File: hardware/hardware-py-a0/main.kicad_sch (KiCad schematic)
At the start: 64 parts, among them J1 Conn_02x08_Odd_Even, J2 USB_C_Receptacle_USB2.0_16P, J3 Conn_02x04_Odd_Even, Q3 AO3401A, Q6 BSS138, Q7 AO3401A, SW1 SW_Push, SW10 SW_Push, SW11 SW_Push, SW12 SW_Push, SW13 SW_Push, SW14 SW_Push, SW15 SW_Push, SW16 SW_Push, SW17 SW_Push, SW18 SW_Push, SW19 SW_Push, SW2 SW_Push, SW20 SW_Push, SW21 Encoder, SW22 RST, SW3 SW_Push, SW4 SW_Push, SW5 SW_Push, SW6 SW_Push, SW7 SW_Push, SW8 SW_Push, SW9 SW_Push, U3 74HC595, U4 ESP32-S3-WROOM-1

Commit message: [dev] py-a0 board files
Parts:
- added C4: 1u, Capacitor_SMD:C_1206_3216Metric, symbol Device:C
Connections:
- net GND: now also C4.2
- net RST: now also C4.1
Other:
- moved on the sheet: SW22
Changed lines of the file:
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@@
 	)
 	(junction
+		(at 147.32 105.41)
+		(diameter 0)
+		(color 0 0 0 0)
+	)
+	(junction
+		(at 139.7 105.41)
+		(diameter 0)
+		(color 0 0 0 0)
+	)
+	(junction
 		(at 190.5 50.8)
 		(diameter 0)
@@
 	)
 	(junction
+		(at 160.02 114.3)
+		(diameter 0)
+		(color 0 0 0 0)
+	)
+	(junction
 		(at 210.82 50.8)
 		(diameter 0)
@@
 	(wire
 		(pts
+			(xy 160.02 114.3) (xy 147.32 114.3)
+		)
+		(stroke
+			(width 0)
+			(type default)
+		)
+	)
+	(wire
+		(pts
 			(xy 71.12 64.77) (xy 71.12 60.96)
 		)
@@
 	(wire
 		(pts
-			(xy 139.7 102.87) (xy 139.7 114.3)
+			(xy 139.7 104.14) (xy 139.7 105.41)
 		)
 		(stroke
@@
 	(wire
 		(pts
+			(xy 139.7 105.41) (xy 139.7 114.3)
+		)
+		(stroke
+			(width 0)
+			(type default)
+		)
+	)
+	(wire
+		(pts
 			(xy 91.44 54.61) (xy 91.44 50.8)
 		)
@@
 	(wire
 		(pts
+			(xy 149.86 105.41) (xy 147.32 105.41)
+		)
+		(stroke
+			(width 0)
+			(type default)
+		)
+	)
+	(wire
+		(pts
 			(xy 124.46 114.3) (xy 127 114.3)
 		)
@@
 	(wire
 		(pts
-			(xy 151.13 114.3) (xy 149.86 114.3)
+			(xy 147.32 105.41) (xy 139.7 105.41)
 		)
 		(stroke
@@
 	(wire
 		(pts
+			(xy 160.02 114.3) (xy 160.02 105.41)
+		)
+		(stroke
+			(width 0)
+			(type default)
+		)
+	)
+	(wire
+		(pts
 			(xy 119.38 102.87) (xy 124.46 102.87)
 		)
@@
 	(wire
 		(pts
+			(xy 147.32 114.3) (xy 147.32 113.03)
+		)
+		(stroke
+			(width 0)
+			(type default)
+		)
+	)
+	(wire
+		(pts
 			(xy 186.69 134.62) (xy 170.18 134.62)
 		)
@@
 	(hierarchical_label "RST"
 		(shape input)
-		(at 139.7 102.87 0)
+		(at 139.7 104.14 90)
 		(fields_autoplaced yes)
 		(effects
@@
 	(symbol
 		(lib_id "Switch:SW_Push")
-		(at 144.78 114.3 0)
+		(at 154.94 105.41 0)
 		(unit 1)
 		(exclude_from_sim no)
@@
 		(fields_autoplaced yes)
 		(property "Reference" "SW22"
-			(at 144.78 106.68 0)
+			(at 154.94 97.79 0)
 			(effects
 				(font
@@
 		)
 		(property "Value" "RST"
-			(at 144.78 109.22 0)
+			(at 154.94 100.33 0)
 			(effects
 				(font
@@
 		)
 		(property "Footprint" "Button_Switch_SMD:SW_SPST_PTS647_Sx38"
-			(at 144.78 109.22 0)
+			(at 154.94 100.33 0)
 			(effects
 				(font
@@
 		)
 		(property "Datasheet" "~"
-			(at 144.78 109.22 0)
+			(at 154.94 100.33 0)
 			(effects
 				(font
@@
 		)
 		(property "Description" "Push button switch, generic, two pins"
-			(at 144.78 114.3 0)
+			(at 154.94 105.41 0)
 			(effects
 				(font
@@
 	(symbol
 		(lib_id "power:GND")
-		(at 151.13 114.3 0)
+		(at 160.02 114.3 0)
 		(mirror y)
 		(unit 1)
@@
 		(dnp no)
 		(property "Reference" "#PWR06"
-			(at 151.13 120.65 0)
+			(at 160.02 120.65 0)
 			(effects
 				(font
@@
 		)
 		(property "Value" "GND"
-			(at 153.67 114.3 0)
+			(at 162.56 114.3 0)
 			(effects
 				(font
@@
 		)
 		(property "Footprint" ""
-			(at 151.13 114.3 0)
+			(at 160.02 114.3 0)
 			(effects
 				(font
@@
 		)
 		(property "Datasheet" ""
-			(at 151.13 114.3 0)
+			(at 160.02 114.3 0)
 			(effects
 				(font
@@
 		)
 		(property "Description" "Power symbol creates a global label with name \"GND\" , ground"
-			(at 151.13 114.3 0)
+			(at 160.02 114.3 0)
 			(effects
 				(font
@@
 					(unit 1)
 				)
+			)
+		)
+	)
+	(symbol
+		(lib_id "Device:C")
+		(at 147.32 109.22 0)
+		(unit 1)
+		(exclude_from_sim no)
+		(in_bom yes)
+		(on_board yes)
+		(dnp no)
+		(property "Reference" "C4"
+			(at 146.558 103.632 0)
+			(effects
+				(font
+					(size 1.27 1.27)
+				)
+				(justify left)
+			)
+		)
+		(property "Value" "1u"
+			(at 148.082 112.268 0)
+			(effects
+				(font
+					(size 1.27 1.27)
+				)
+				(justify left)
+			)
+		)
+		(property "Footprint" "Capacitor_SMD:C_1206_3216Metric"
+			(at 148.2852 113.03 0)
+			(effects
+				(font
+					(size 1.27 1.27)
+				)
+				(hide yes)
+			)
+		)
+		(property "Datasheet" "~"
+			(at 147.32 109.22 0)
+			(effects
+				(font
+					(size 1.27 1.27)
+				)
+				(hide yes)
+			)
+		)
+		(property "Description" "Unpolarized capacitor"
+			(at 147.32 109.22 0)
+			(effects
+				(font
+					(size 1.27 1.27)
+				)
+				(hide yes)
+			)
+		)
+		(pin "2"
+		)
+		(pin "1"
+		)
+		(instances
+			(project "numcalcium"
+				(path "/842c0813-91d3-4f68-bc1f-ac3ce07be478/b6a1d74e-f5bd-4c1c-9567-b593baf30f34"
+					(reference "C4")
+					(unit 1)
+				)

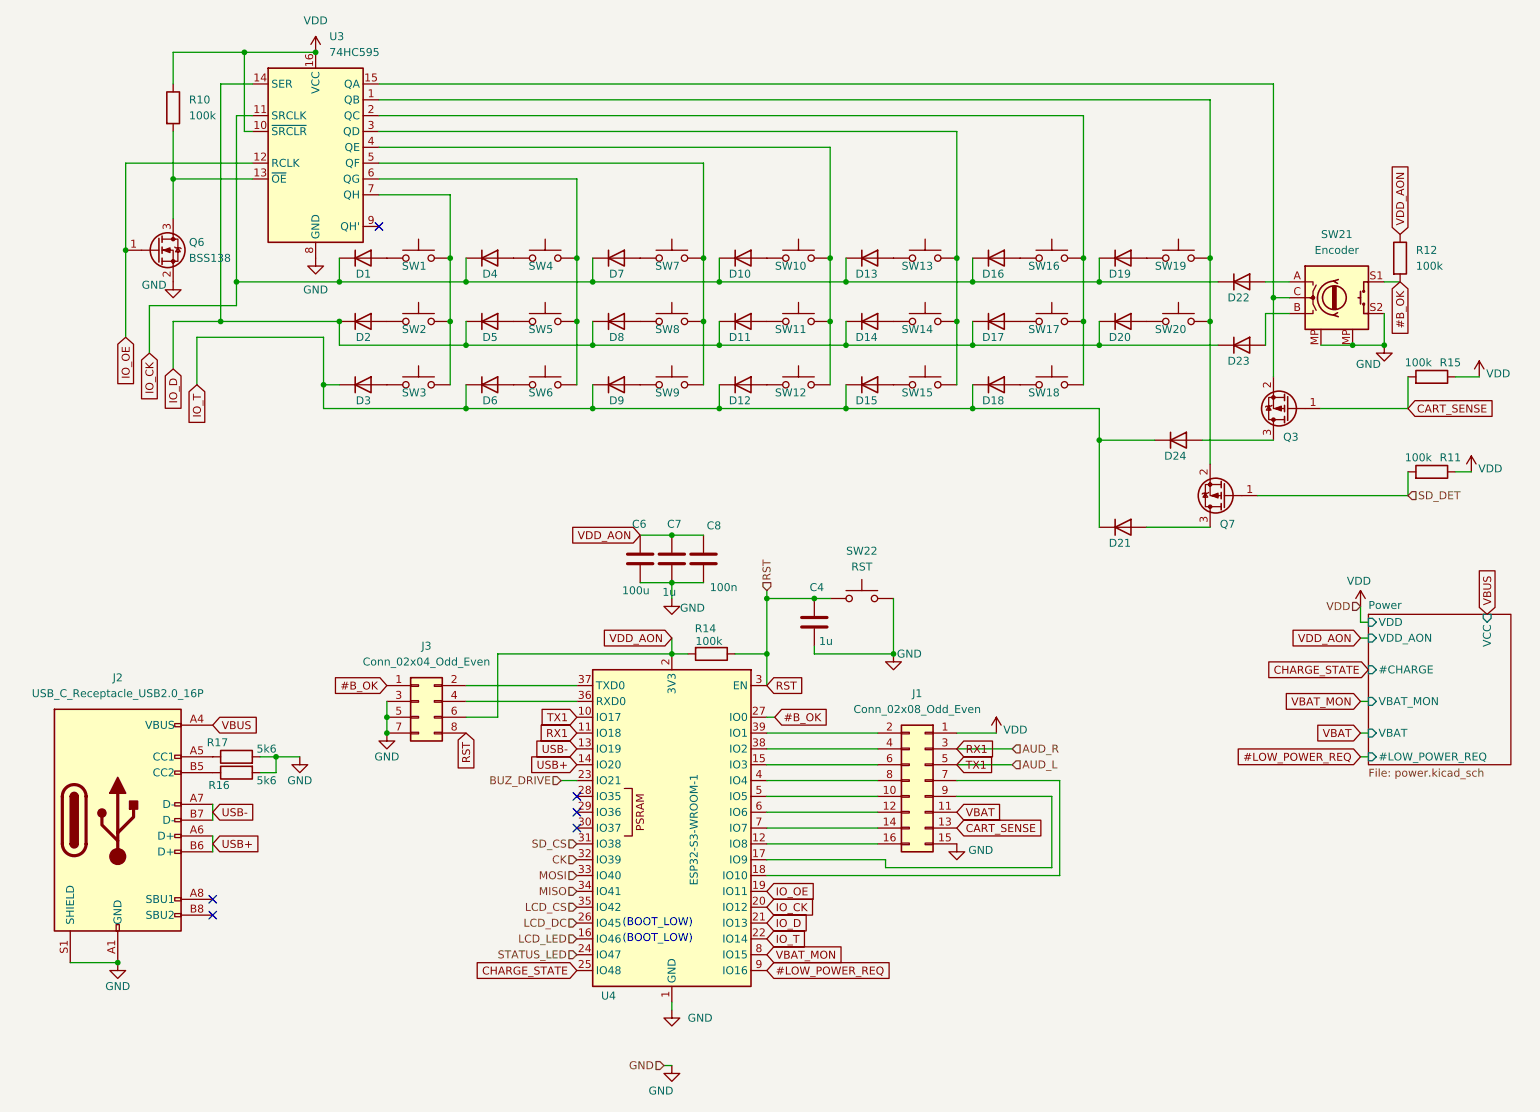
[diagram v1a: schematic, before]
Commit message: hardware: py/a0 revision 1.1 using FFC connectors
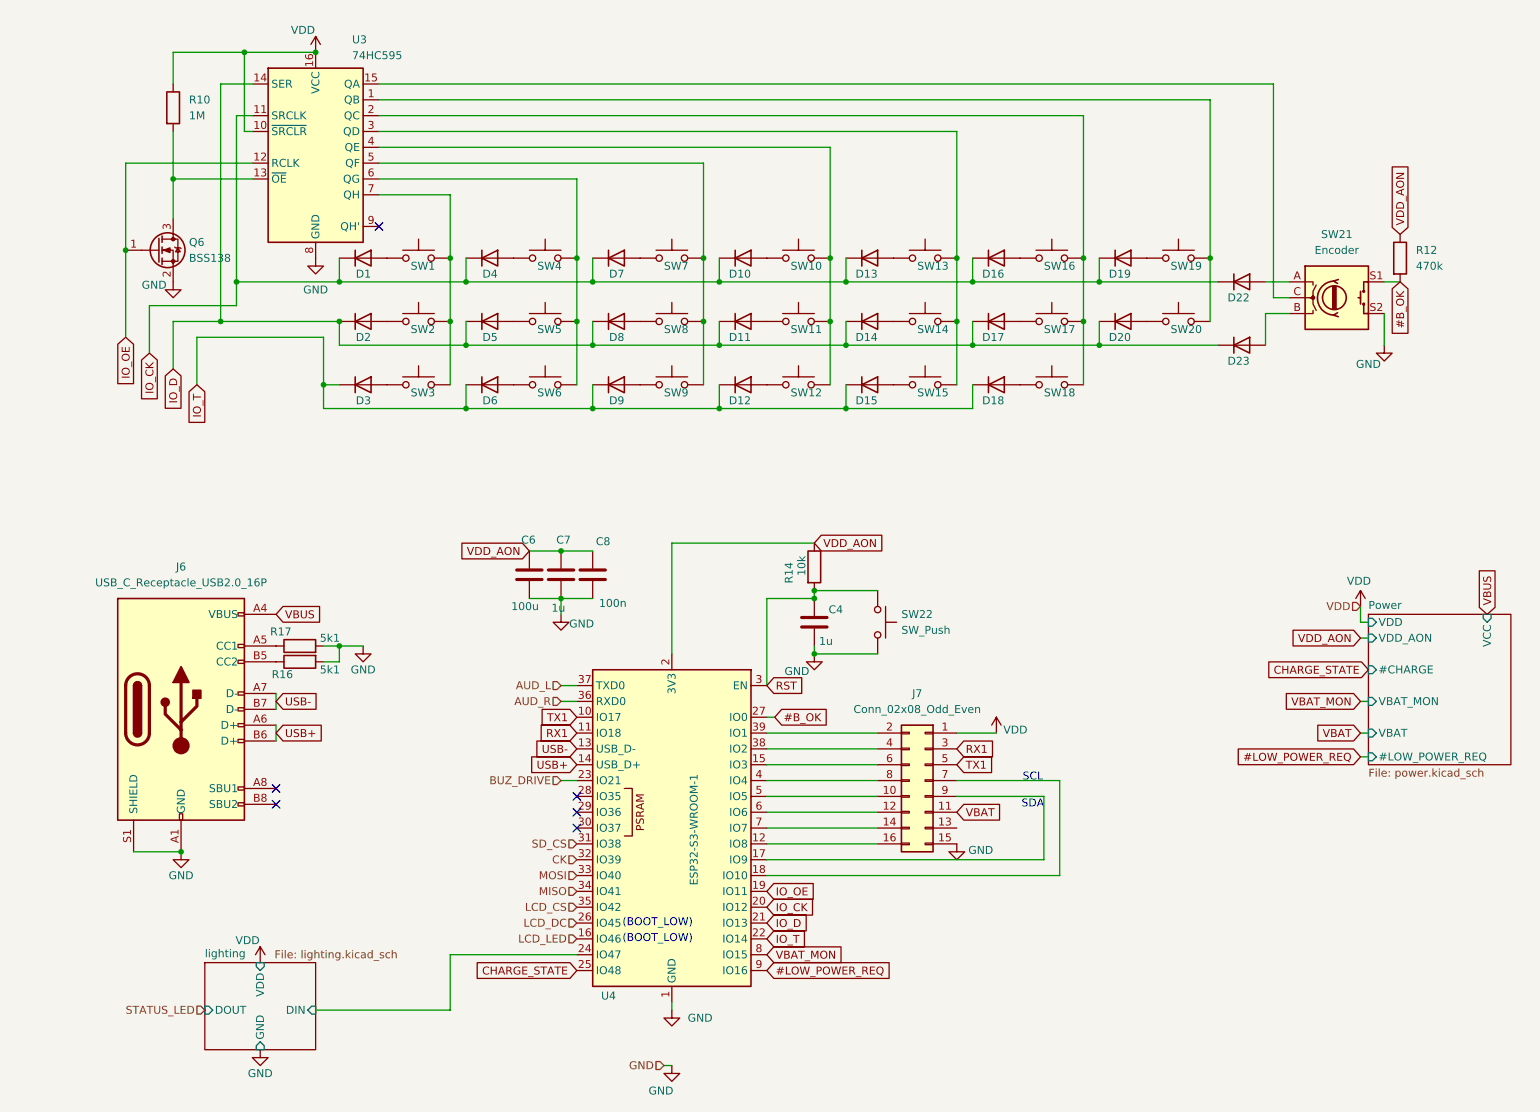
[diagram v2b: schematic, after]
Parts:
- removed D21, D24: D, Diode_SMD:D_0805_2012Metric_Pad1.15x1.40mm_HandSolder, symbol Device:D
- removed J3: Conn_02x04_Odd_Even, Connector_PinHeader_1.27mm:PinHeader_2x04_P1.27mm_Vertical_SMD, symbol Connector_Generic:Conn_02x04_Odd_Even
- removed Q3, Q7: AO3401A, Package_TO_SOT_SMD:SOT-23, symbol Transistor_FET:AO3401A
- removed R11, R15: 100k, Resistor_SMD:R_0805_2012Metric_Pad1.20x1.40mm_HandSolder, symbol Device:R
- C6: footprint Capacitor_SMD:C_Elec_5x5.4 -> Capacitor_SMD:C_2220_5750Metric
- D1, D10, D11, D12, D13, D14, D15, D16, D17, D18, D19, D2, D20, D22, D23, D3, D4, D5, D6, D7, D8, D9: footprint Diode_SMD:D_0805_2012Metric_Pad1.15x1.40mm_HandSolder -> Diode_SMD:D_1206_3216Metric
- R10: value 100k -> 1M
- R12: value 100k -> 470k
- R14: value 100k -> 10k
- R16, R17: value 5k6 -> 5k1
- SW1, SW10, SW11, SW12, SW13, SW14, SW15, SW16, SW17, SW18, SW19, SW2, SW20, SW3, SW4, SW5, SW6, SW7, SW8, SW9: footprint footprints:Combo_MechanicalSwitch -> footprints:CherrySocket_MechanicalSwitch
- SW22: value RST -> SW_Push
- renumbered J2 to J6, J1 to J7
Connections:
- net GND: no longer SW21.MP (MOUNT)
- net RST: now also R14.2; no longer R14.1
- net STATUS_LED: no longer U4.24 (IO47)
- net VDD_AON: now also R14.1; no longer R14.2
- net at D7.2 (A): now also SW7.2; no longer SW7.1
- net at D8.2 (A): now also SW8.2; no longer SW8.1
- net at SW1.1: now also SW2.1, SW3.1, U3.7 (QH); no longer D1.2 (A)
- net at SW11.1: now also SW10.1, SW12.1, U3.4 (QE); no longer D11.2 (A)
- net at SW4.1: now also SW5.1, SW6.1, U3.6 (QG); no longer D4.2 (A)
- net at SW14.1: now also SW13.1, SW15.1, U3.3 (QD); no longer D14.2 (A)
- net at D13.2 (A): now also SW13.2; no longer SW13.1
- net at D6.2 (A): now also SW6.2; no longer SW6.1
- net at SW19.1: now also SW20.1, U3.1 (QB); no longer D19.2 (A)
- net at D20.2 (A): now also SW20.2; no longer SW20.1
- net at D15.2 (A): now also SW15.2; no longer SW15.1
- net at D5.2 (A): now also SW5.2; no longer SW5.1
- net at D2.2 (A): now also SW2.2; no longer SW2.1
- net at SW16.1: now also SW17.1, SW18.1, U3.2 (QC); no longer D16.2 (A)
- net at SW9.1: now also SW7.1, SW8.1, U3.5 (QF); no longer D9.2 (A)
- net at D18.2 (A): now also SW18.2; no longer SW18.1
- net at D3.2 (A): now also SW3.2; no longer SW3.1
- net at D17.2 (A): now also SW17.2; no longer SW17.1
- net at D10.2 (A): now also SW10.2; no longer SW10.1
- net AUD_R: now reaches U4.36 (RXD0)
- net AUD_L: now reaches U4.37 (TXD0)
- net at D12.2 (A): now also SW12.2; no longer SW12.1
- net CART_SENSE: no longer names the net of J7.13 (Pin_13)
- new net: D1.2 (A), SW1.2
- new net: D11.2 (A), SW11.2
- new net: D4.2 (A), SW4.2
- new net: D14.2 (A), SW14.2
- new net: D19.2 (A), SW19.2
- new net: D16.2 (A), SW16.2
- new net: D9.2 (A), SW9.2
- new net lighting/DIN: U4.24 (IO47)
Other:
- added sheet lighting (lighting.kicad_sch)
- note added: "SCL"
- note added: "SDA"
- company: (none) -> MOTIV.PW
- title: (none) -> Main
- moved on the sheet: C6, C7, C8, J6, R14, R16, R17

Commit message: hw: power management begin
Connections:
- net AUD_L: no longer names the net of U4.37 (TXD0)
- net AUD_R: no longer names the net of U4.36 (RXD0)
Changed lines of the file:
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@@
+	)
+	(junction
+		(at 96.52 124.46)
+		(diameter 0)
+		(color 0 0 0 0)
 	)
 	(junction
@@
 	(junction
 		(at 190.5 60.96)
+		(diameter 0)
+		(color 0 0 0 0)
+	)
+	(junction
+		(at 96.52 127)
 		(diameter 0)
 		(color 0 0 0 0)
@@
 	(wire
 		(pts
-			(xy 109.22 119.38) (xy 106.68 119.38)
+			(xy 93.98 127) (xy 96.52 127)
 		)
 		(stroke
@@
 	(wire
 		(pts
+			(xy 95.25 121.92) (xy 96.52 121.92)
+		)
+		(stroke
+			(width 0)
+			(type default)
+		)
+	)
+	(wire
+		(pts
 			(xy 172.72 54.61) (xy 193.04 54.61)
 		)
@@
 	(wire
 		(pts
+			(xy 95.25 129.54) (xy 96.52 129.54)
+		)
+		(stroke
+			(width 0)
+			(type default)
+		)
+	)
+	(wire
+		(pts
 			(xy 139.7 144.78) (xy 157.48 144.78)
 		)
@@
 	(wire
 		(pts
+			(xy 96.52 127) (xy 109.22 127)
+		)
+		(stroke
+			(width 0)
+			(type default)
+		)
+	)
+	(wire
+		(pts
 			(xy 129.54 60.96) (xy 129.54 71.12)
 		)
@@
 	(wire
 		(pts
+			(xy 96.52 121.92) (xy 96.52 124.46)
+		)
+		(stroke
+			(width 0)
+			(type default)
+		)
+	)
+	(wire
+		(pts
 			(xy 193.04 60.96) (xy 193.04 64.77)
 		)
@@
 	(wire
 		(pts
-			(xy 109.22 121.92) (xy 106.68 121.92)
-		)
-		(stroke
-			(width 0)
-			(type default)
-		)
-	)
-	(wire
-		(pts
 			(xy 88.9 162.56) (xy 109.22 162.56)
 		)
@@
 	(wire
 		(pts
+			(xy 93.98 124.46) (xy 96.52 124.46)
+		)
+		(stroke
+			(width 0)
+			(type default)
+		)
+	)
+	(wire
+		(pts
 			(xy 152.4 74.93) (xy 152.4 71.12)
 		)
@@
 	(wire
 		(pts
+			(xy 96.52 129.54) (xy 96.52 127)
+		)
+		(stroke
+			(width 0)
+			(type default)
+		)
+	)
+	(wire
+		(pts
 			(xy 152.4 54.61) (xy 152.4 50.8)
 		)
@@
 	(wire
 		(pts
+			(xy 96.52 124.46) (xy 109.22 124.46)
+		)
+		(stroke
+			(width 0)
+			(type default)
+		)
+	)
+	(wire
+		(pts
 			(xy 124.46 96.52) (xy 147.32 96.52)
 		)
@@
 	(wire
 		(pts
-			(xy 106.68 134.62) (xy 109.22 134.62)
+			(xy 104.14 134.62) (xy 109.22 134.62)
 		)
 		(stroke
@@
 	(global_label "TX1"
 		(shape input)
-		(at 109.22 124.46 180)
-		(fields_autoplaced yes)
-		(effects
-			(font
-				(size 1.27 1.27)
-			)
-			(justify right)
-		)
-		(property "Intersheetrefs" "${INTERSHEET_REFS}"
-			(at 102.8482 124.46 0)
+		(at 93.98 124.46 180)
+		(fields_autoplaced yes)
+		(effects
+			(font
+				(size 1.27 1.27)
+			)
+			(justify right)
+		)
+		(property "Intersheetrefs" "${INTERSHEET_REFS}"
+			(at 87.6082 124.46 0)
 			(effects
 				(font
@@
 	(global_label "RX1"
 		(shape input)
-		(at 109.22 127 180)
-		(fields_autoplaced yes)
-		(effects
-			(font
-				(size 1.27 1.27)
-			)
-			(justify right)
-		)
-		(property "Intersheetrefs" "${INTERSHEET_REFS}"
-			(at 102.5458 127 0)
+		(at 93.98 127 180)
+		(fields_autoplaced yes)
+		(effects
+			(font
+				(size 1.27 1.27)
+			)
+			(justify right)
+		)
+		(property "Intersheetrefs" "${INTERSHEET_REFS}"
+			(at 87.3058 127 0)
 			(effects
 				(font
@@
 	(hierarchical_label "AUD_L"
 		(shape input)
-		(at 106.68 119.38 180)
+		(at 95.25 121.92 180)
 		(fields_autoplaced yes)
 		(effects
@@
 	(hierarchical_label "AUD_R"
 		(shape input)
-		(at 106.68 121.92 180)
+		(at 95.25 129.54 180)
 		(fields_autoplaced yes)
 		(effects
@@
 	(hierarchical_label "BUZ_DRIVE"
 		(shape input)
-		(at 106.68 134.62 180)
-		(fields_autoplaced yes)
-		(effects
+		(at 104.14 134.62 180)
+		(fields_autoplaced yes)
+		(effects
